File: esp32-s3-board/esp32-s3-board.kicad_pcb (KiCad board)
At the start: 2 copper layers, 25.4 x 55.9 mm, 26 parts, among them J1 MC-314C-4P16, J2 Conn_01x22, J3 Conn_01x22, Q1 UMH3N, U1 USBLC6-2P6, U2 LDL1117S33R, U3 CP2102N-Axx-xQFN28, U4 ESP32-S3-WROOM-1

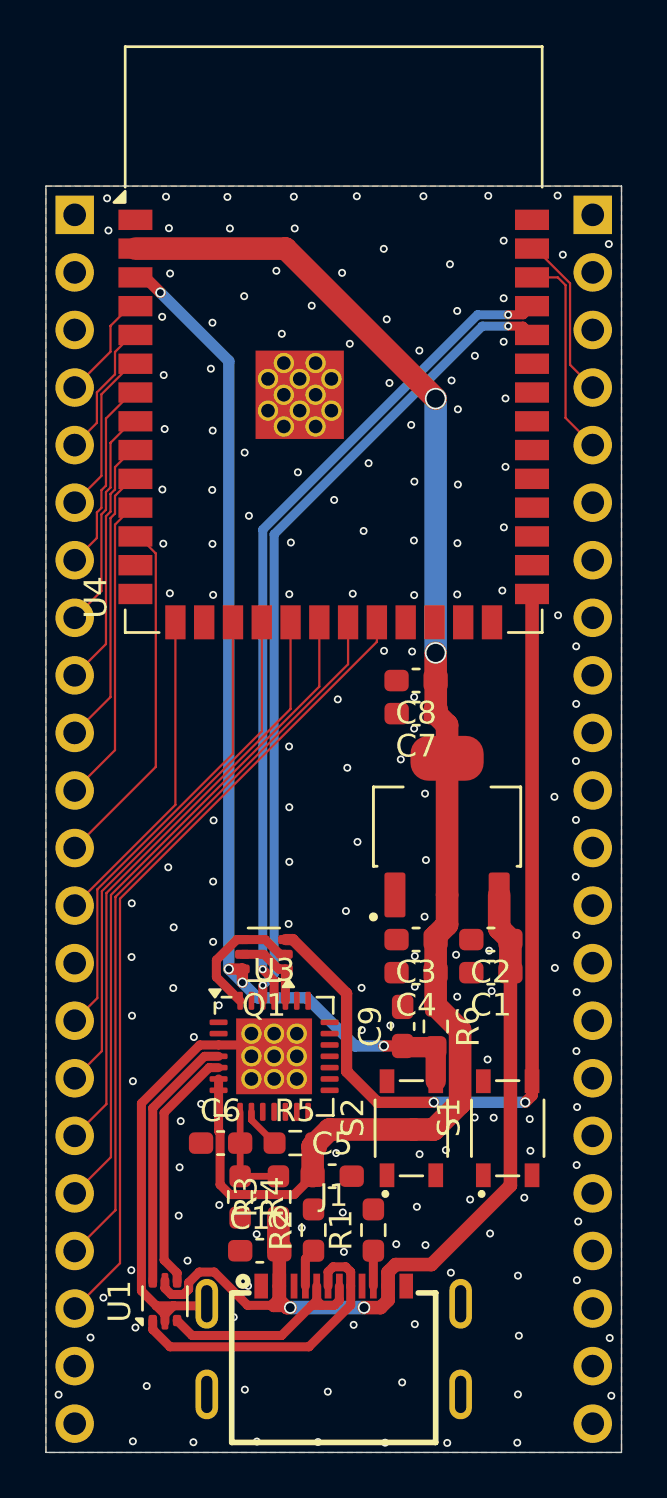
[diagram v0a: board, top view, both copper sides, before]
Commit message: Make vias bigger and add teardrop
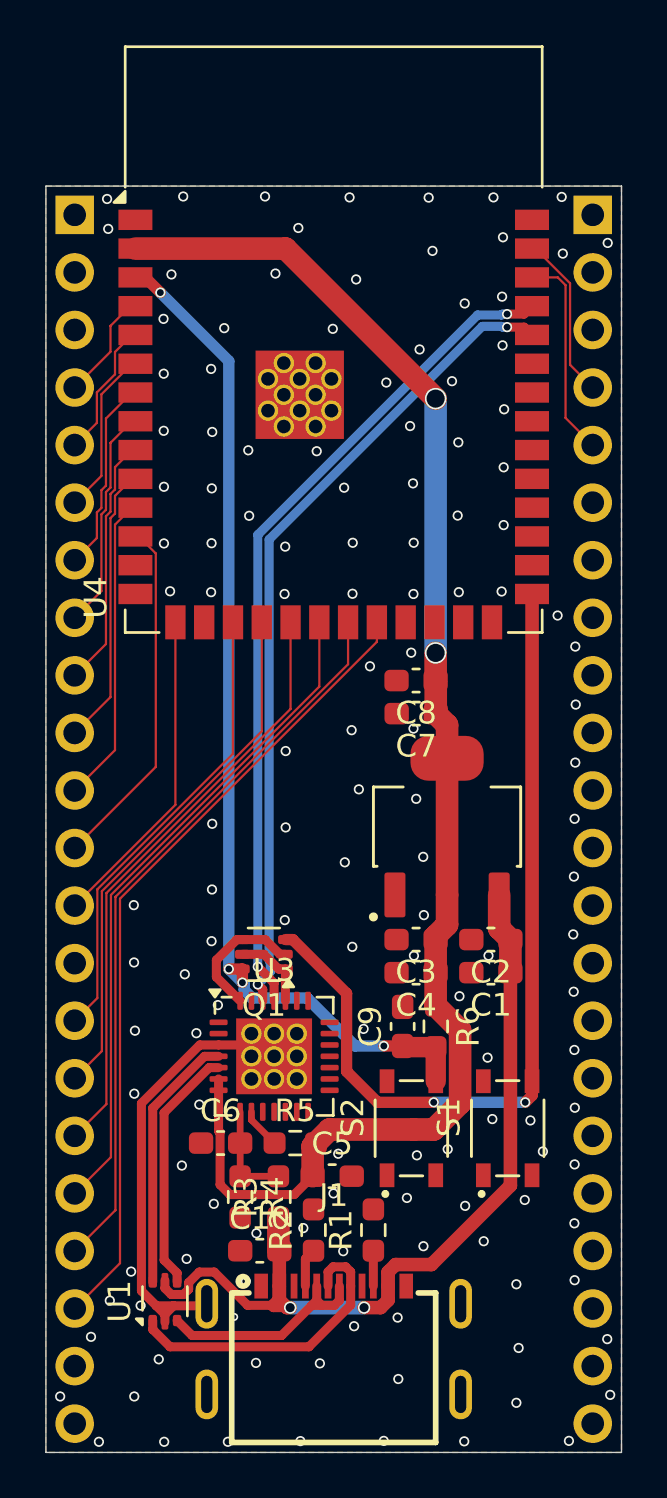
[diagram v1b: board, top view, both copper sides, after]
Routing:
- net GND: vias 167 -> 140
